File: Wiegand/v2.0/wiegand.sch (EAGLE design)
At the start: 55 parts, among them CON1 SPI, Q1 BSP75, Q2 BSP75, Q4 BSP75, Q7 BSP75, X3 16MHz, X4 MINI-USB

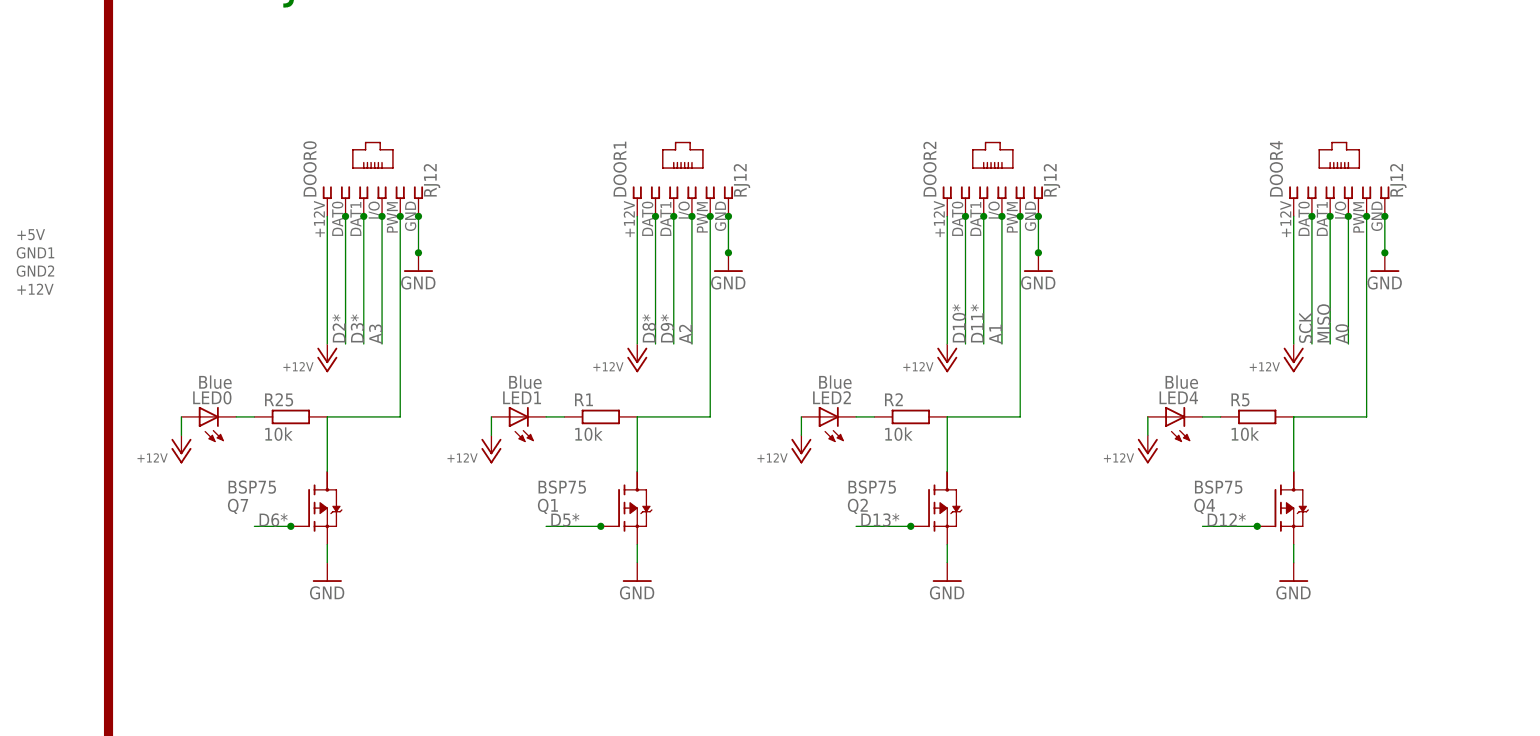
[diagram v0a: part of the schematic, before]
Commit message: Add relay card and integrated bioreactor
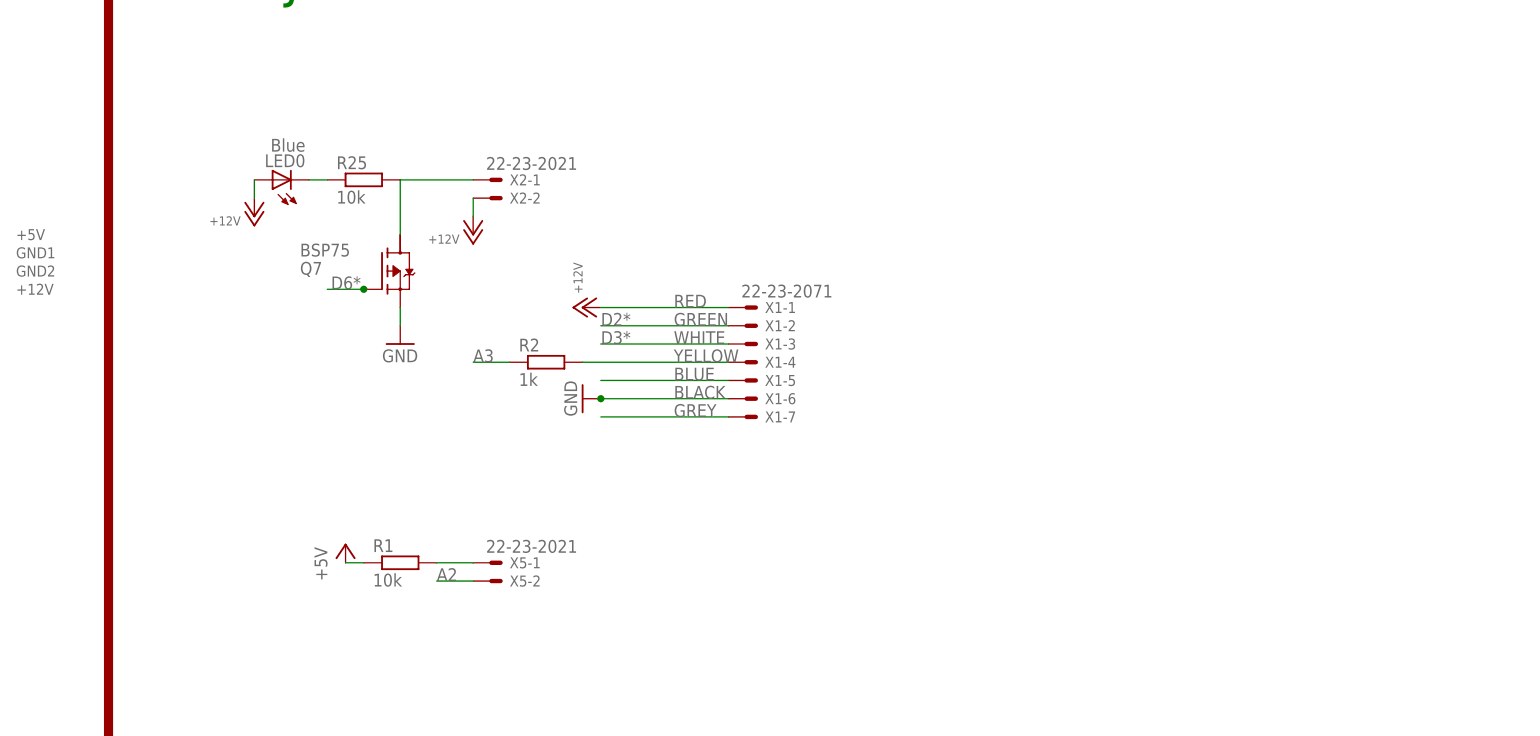
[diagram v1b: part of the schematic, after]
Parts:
- removed DOOR0, DOOR1, DOOR2, DOOR4: RJ12, lpatiny:RJ12STR-WIEGAND
- removed LED1, LED2, LED4: Blue, SparkFun:LED1206
- removed Q1, Q2, Q4: BSP75, infineon:BSP613P
- removed R5: 10k, rcl:R-EU_R0805
- added X1: 22-23-2071, con-molex:22-23-2071
- added X2, X5: 22-23-2021, con-molex:22-23-2021
- R2: value 10k -> 1k
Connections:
- removed net N$31: DOOR4.5, Q4.D@1, R5.2
- removed net N$7: DOOR2.5, Q2.D@1, R2.2
- removed net N$9: LED4.C, R5.1
- new net N$4: X1-7.S
- net +12V: now also X2-2.S; no longer DOOR0.1, DOOR1.1, DOOR2.1, DOOR4.1, LED1.A, LED2.A, LED4.A
- net +5V: now also R1.1
- net A0: no longer DOOR4.4
- net A1: no longer DOOR2.4
- net A2: now also X5-2.S; no longer DOOR1.4
- net A3: now also R2.1; no longer DOOR0.4
- net D10*: no longer DOOR2.2
- net D11*: no longer DOOR2.3
- net D12*: no longer Q4.G
- net D13*: no longer Q2.G
- net D2*: no longer DOOR0.2
- net D3*: no longer DOOR0.3
- net D5*: no longer Q1.G
- net D8*: no longer DOOR1.2
- net D9*: no longer DOOR1.3
- net GND: no longer DOOR0.6, DOOR1.6, DOOR2.6, DOOR4.6, Q1.S, Q2.S, Q4.S
- net MISO: no longer DOOR4.3
- net N$23: now also X2-1.S; no longer DOOR0.5
- net N$3: now also X1-5.S; no longer DOOR1.5, Q1.D@1, R1.2
- net N$5: now also R1.2, X5-1.S; no longer LED1.C, R1.1
- net N$6: now also R2.2, X1-4.S; no longer LED2.C, R2.1
- net SCK: no longer DOOR4.2
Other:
- note added: "BLACK"
- note added: "BLUE"
- note added: "GREEN"
- note added: "GREY"
- note added: "RED"
- note added: "WHITE"
- note added: "YELLOW"
- moved on the sheet: LED0, Q7, R1, R2, R25
